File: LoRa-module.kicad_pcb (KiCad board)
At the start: 4 copper layers, 14.3 x 13 mm, 27 parts, among them J1 5035661102, M1 0900FM15K0039001E, U1 SX1262IMLTRT, U2 IPEX-1

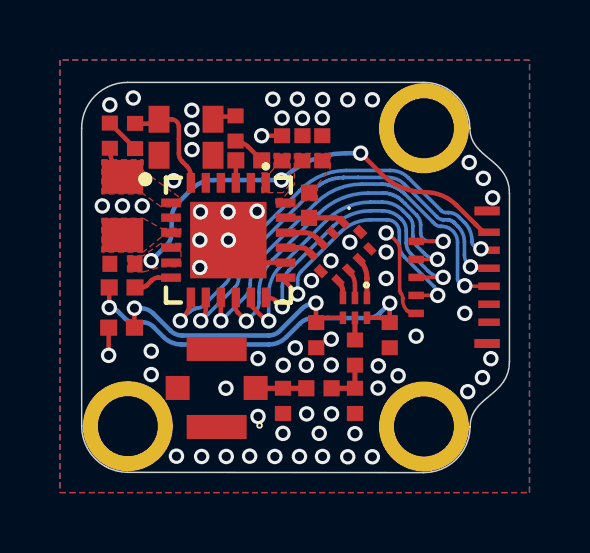
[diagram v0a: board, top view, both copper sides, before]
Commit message: Updated FPC pinout
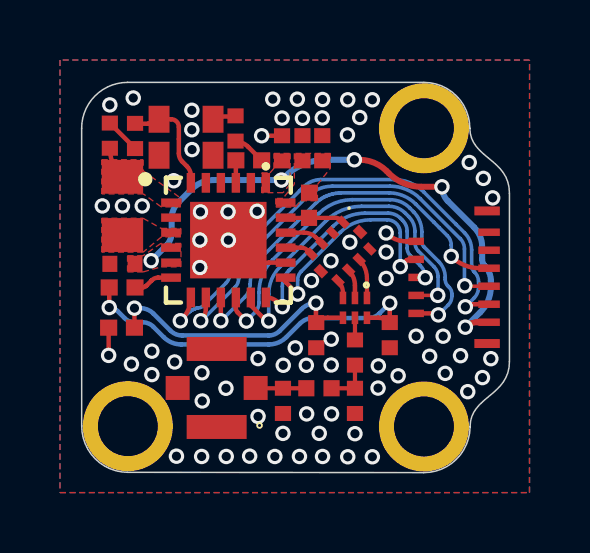
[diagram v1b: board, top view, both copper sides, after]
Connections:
- J1 pad 1: GND -> +3V3
- J1 pad 10: /MISO -> /RF_SW
- J1 pad 11: +3V3 -> GND
- J1 pad 2: /RF_SW -> /MISO
- J1 pad 3: GND -> /DIO1
- J1 pad 4: /NSS -> /MOSI
- J1 pad 5: /NRESET -> /BUSY
- J1 pad 7: /BUSY -> /NRESET
- J1 pad 8: /MOSI -> /NSS
- J1 pad 9: /DIO1 -> GND
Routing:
- net +3V3: track 14.2 -> 18.1 mm, vias 3 -> 5
- net /RF_SW: track 15.2 -> 12.9 mm
- net /MISO: track 11.3 -> 13.6 mm
- net /DIO1: track 14.8 -> 16.7 mm
- net /NSS: track 8.74 -> 7.42 mm
- net /NRESET: track 14.2 -> 13.0 mm
- net /SCK: track 9.77 -> 8.75 mm
- net /MOSI: track 10.6 -> 11.6 mm
- net GND: vias 64 -> 73
- added copper zone on In3.Cu, net GND
- added copper zone on In4.Cu, net GND
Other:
- copper layers 4 -> 6
